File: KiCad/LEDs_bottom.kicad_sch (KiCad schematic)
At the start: 0 parts

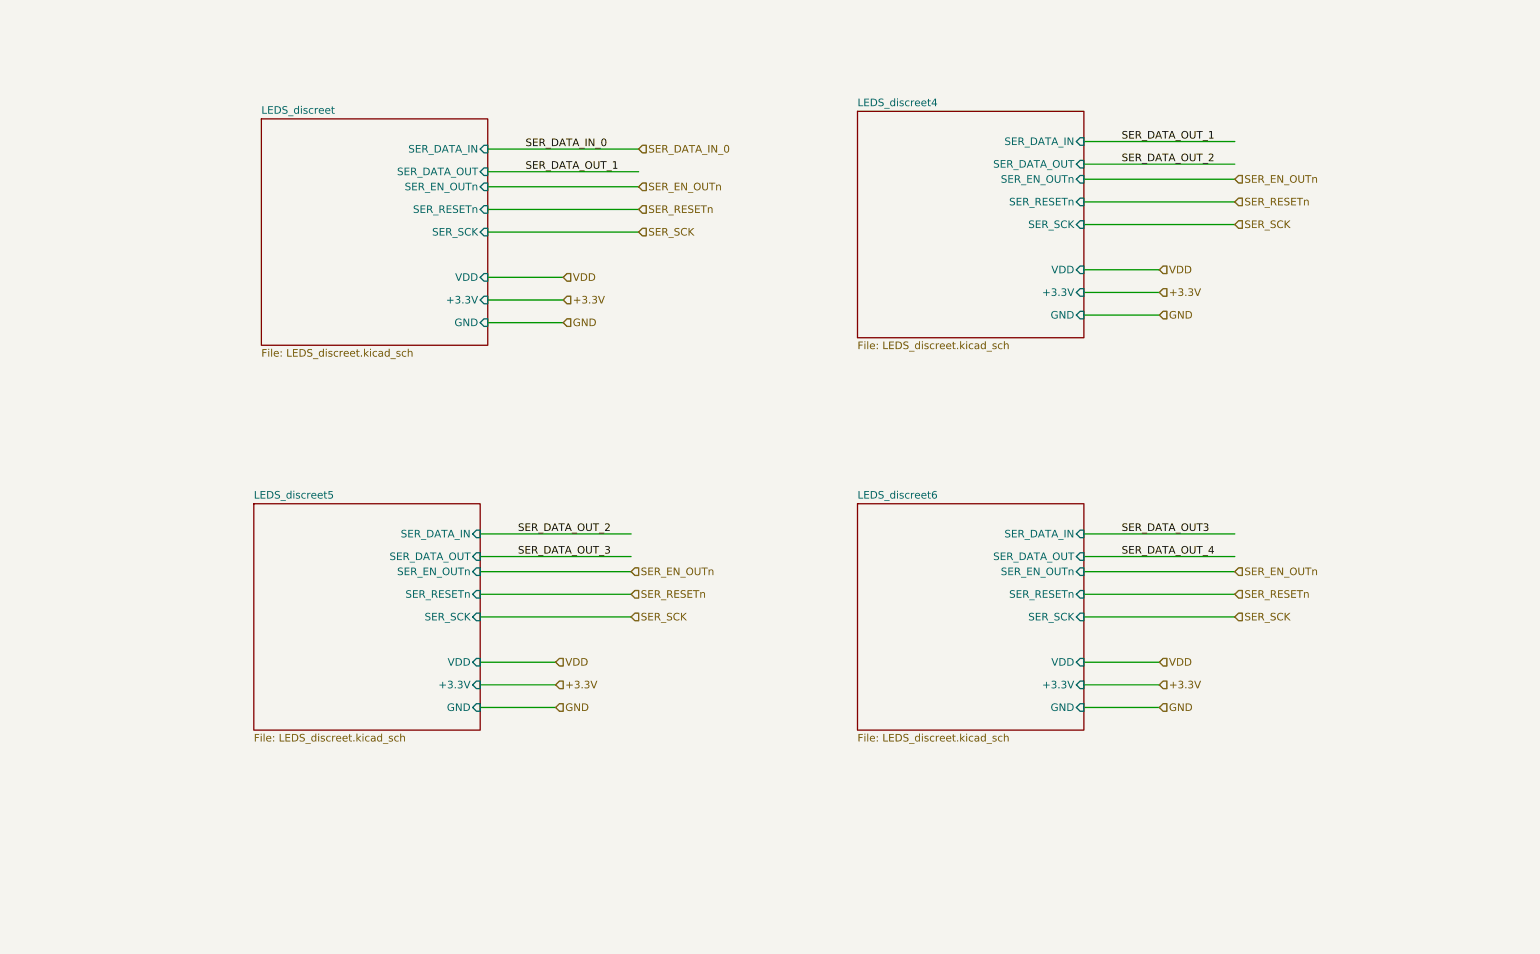
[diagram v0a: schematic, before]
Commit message: Ready for PCB layout with discreet LEDs
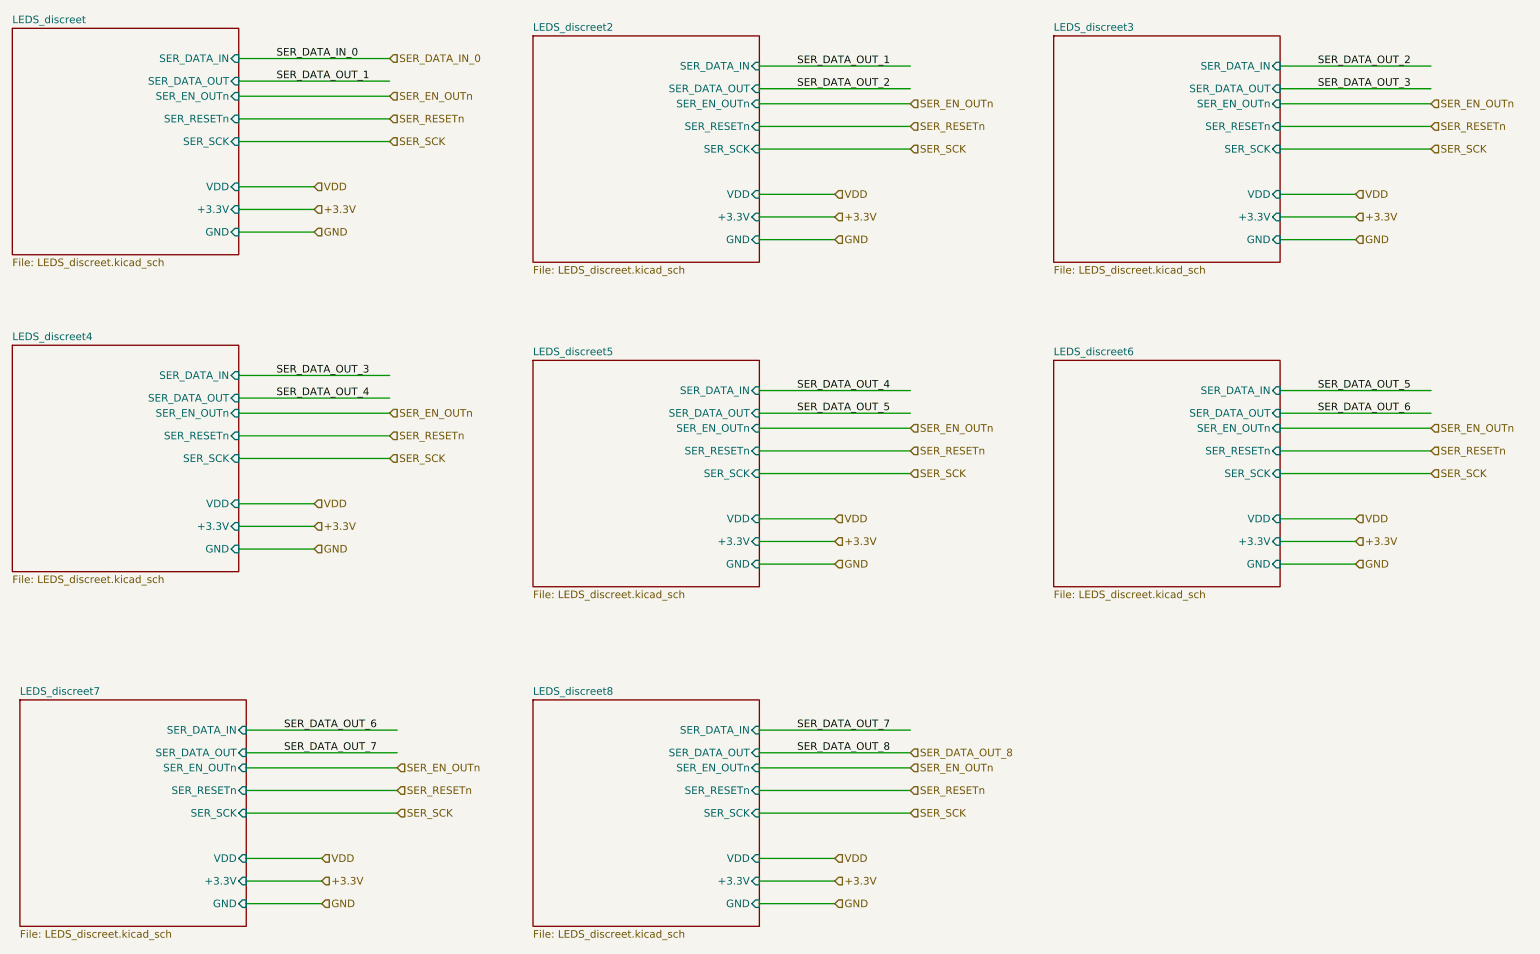
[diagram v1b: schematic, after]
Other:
- added sheet LEDS_discreet2 (LEDS_discreet.kicad_sch)
- added sheet LEDS_discreet3 (LEDS_discreet.kicad_sch)
- added sheet LEDS_discreet7 (LEDS_discreet.kicad_sch)
- added sheet LEDS_discreet8 (LEDS_discreet.kicad_sch)
